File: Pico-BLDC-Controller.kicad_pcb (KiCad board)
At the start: 4 copper layers, 115 x 55 mm, 161 parts, among them J2 Heat Mat, J3 I2C CONN, J4 USB_C_Receptacle_USB2.0_14P, J5 SM03B-SRSS-TB, J6 Conn_01x05, J7 Conn_01x02, J8 Conn_01x03, J9 USB_C_Receptacle, Q1 DMN3053L-7, Q2 SIR680LDP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

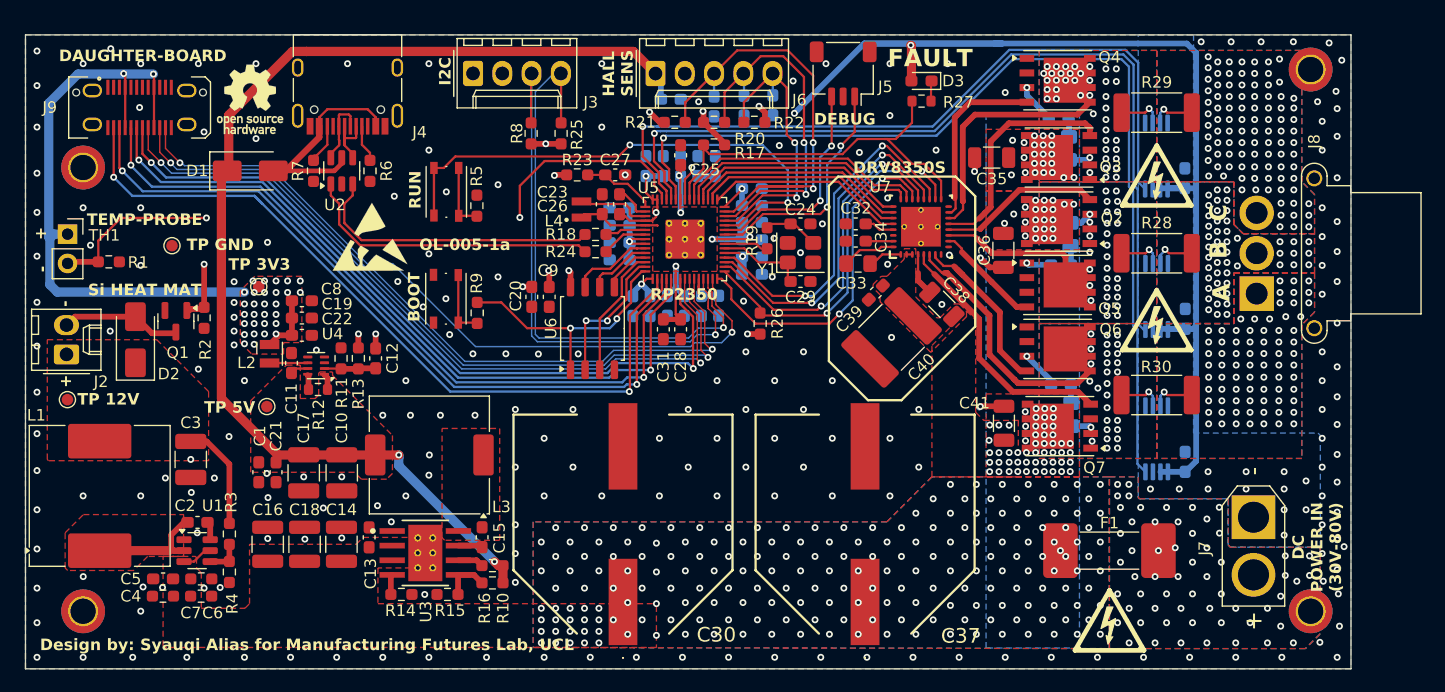
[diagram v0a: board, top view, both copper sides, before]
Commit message: increase board size and more vias
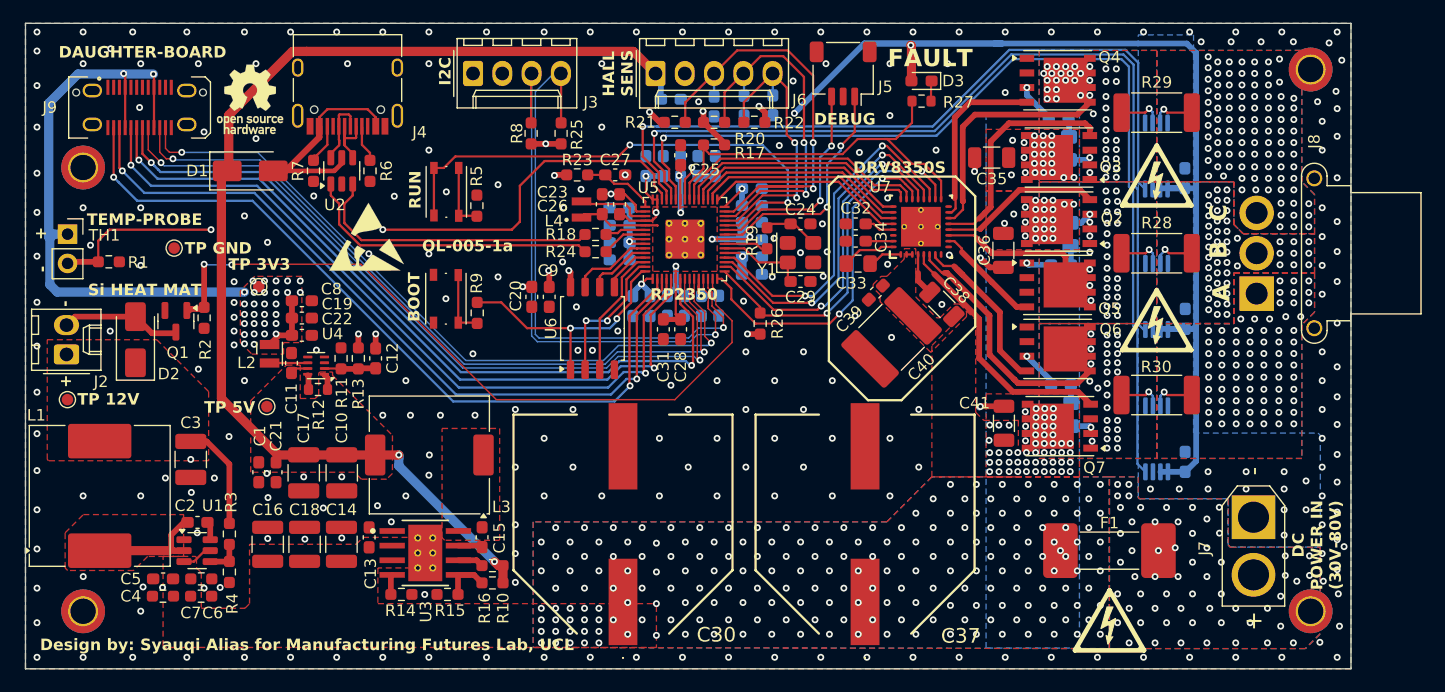
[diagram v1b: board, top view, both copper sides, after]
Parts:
- moved REF** 0.30 mm to (123.0, 60.1)
- moved TP_GND1 0.28 mm to (106.3, 61.1)
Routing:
- net /GPIO10: track 60.1 -> 64.4 mm, vias 3 -> 2
- net /CHA_B: track 65.3 -> 64.4 mm
- net /GPIO3: track 64.0 -> 64.6 mm
- net /GPIO7: track 64.2 -> 63.6 mm
- net GND: vias 230 -> 267
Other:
- board size 115 x 55 mm -> 115 x 56 mm

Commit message: added date on silkscreen
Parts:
- moved C34 0.19 mm to (165.4, 60.6)
- moved C33 0.07 mm to (165.6, 62.5)
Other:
- board text added: "29/08/25"
